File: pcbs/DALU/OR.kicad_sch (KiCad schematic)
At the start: 24 parts

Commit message: Rethinking some design
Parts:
- added U501: 74HCT541, Package_DIP:DIP-20_W7.62mm_Socket, symbol 74xx:74HCT541
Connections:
- net GND: now also U501.10 (GND)
- net OR0: no longer names the net of D501.1 (K), D502.1 (K), R501.1
- net OR0: now also U501.2 (A0)
- net OR1: no longer names the net of D503.1 (K), D504.1 (K), R502.1
- net OR1: now also U501.3 (A1)
- net OR2: no longer names the net of D505.1 (K), D506.1 (K), R503.1
- net OR2: now also U501.4 (A2)
- net OR3: no longer names the net of D507.1 (K), D508.1 (K), R504.1
- net OR3: now also U501.5 (A3)
- net OR4: no longer names the net of D509.1 (K), D510.1 (K), R505.1
- net OR4: now also U501.6 (A4)
- net OR5: no longer names the net of D511.1 (K), D512.1 (K), R506.1
- net OR5: now also U501.7 (A5)
- net OR6: no longer names the net of D513.1 (K), D514.1 (K), R507.1
- net OR6: now also U501.8 (A6)
- net OR7: no longer names the net of D515.1 (K), D516.1 (K), R508.1
- net OR7: now also U501.9 (A7)
- new net +5V: U501.20 (VCC)
- new net ~{ENABLE_{OR}}: U501.1 (G1), U501.19 (G2)

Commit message: Doing some rethinking
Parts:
- removed U501: 74HCT541, Package_DIP:DIP-20_W7.62mm_Socket, symbol 74xx:74HCT541
- added U601: 74HC245, Package_SO:SOIC-20W_7.5x12.8mm_P1.27mm, symbol 74xx:74HC245
- renumbered D501 to D601, D502 to D602, D503 to D603, D504 to D604, D505 to D605, D506 to D606, D507 to D607, D508 to D608, D509 to D609, D510 to D610, D511 to D611, D512 to D612, D513 to D613, D514 to D614, D515 to D615, D516 to D616, R501 to R601, R502 to R602, R503 to R603, R504 to R604, R505 to R605, R506 to R606, R507 to R607, R508 to R608
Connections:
- net +5V: now also U601.20 (VCC)
- net GND: now also U601.10 (GND)
- net at D613.1 (K), D614.1 (K), R607.1: now also U601.8 (A6)
- net at D605.1 (K), D606.1 (K), R603.1: now also U601.4 (A2)
- net at D603.1 (K), D604.1 (K), R602.1: now also U601.3 (A1)
- net at D611.1 (K), D612.1 (K), R606.1: now also U601.7 (A5)
- net at D615.1 (K), D616.1 (K), R608.1: now also U601.9 (A7)
- net at D607.1 (K), D608.1 (K), R604.1: now also U601.5 (A3)
- net at D601.1 (K), D602.1 (K), R601.1: now also U601.2 (A0)
- net at D609.1 (K), D610.1 (K), R605.1: now also U601.6 (A4)

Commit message: Starting to think about decoding etc.
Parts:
- renumbered D601 to D701, D602 to D702, D603 to D703, D604 to D704, D605 to D705, D606 to D706, D607 to D707, D608 to D708, D609 to D709, D610 to D710, D611 to D711, D612 to D712, D613 to D713, D614 to D714, D615 to D715, D616 to D716, R601 to R701, R602 to R702, R603 to R703, R604 to R704, R605 to R705, R606 to R706, R607 to R707, R608 to R708, U601 to U701

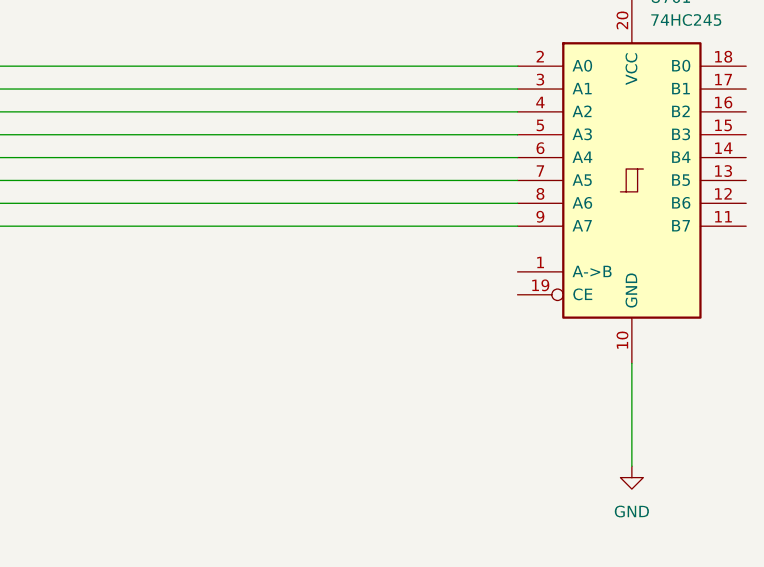
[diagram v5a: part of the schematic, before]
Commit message: Starting to do the routing. Schematic not yet complete, though
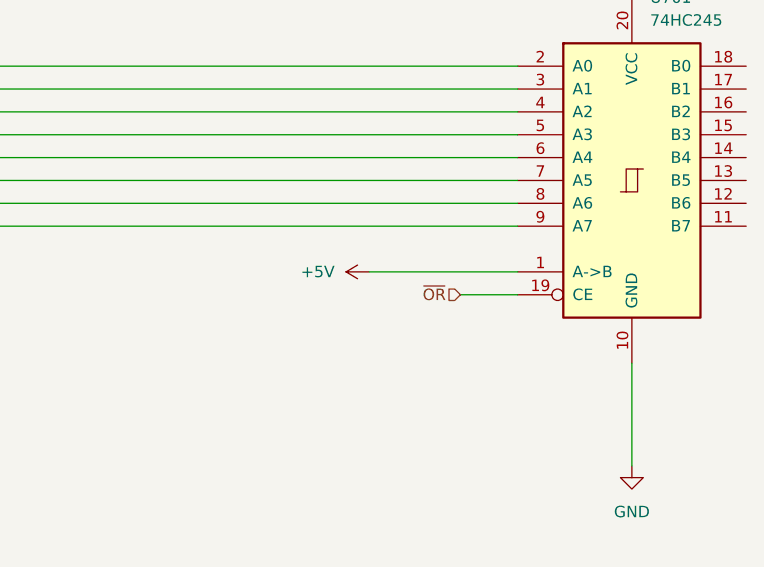
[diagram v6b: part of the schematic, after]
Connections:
- net +5V: now also U701.1 (A->B)
- net ~{OR}: now reaches U701.19 (CE)
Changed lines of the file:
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@@
+    (stroke (width 0) (type default) (color 0 0 0 0))
+  )
+  (wire (pts (xy 214.63 68.58) (xy 220.98 68.58))
     (stroke (width 0) (type default) (color 0 0 0 0))
   )
   (wire (pts (xy 83.82 52.07) (xy 91.44 52.07))
+    (stroke (width 0) (type default) (color 0 0 0 0))
+  )
+  (wire (pts (xy 204.47 66.04) (xy 220.98 66.04))
     (stroke (width 0) (type default) (color 0 0 0 0))
   )
@@
   )
   (hierarchical_label "B[0..7]" (shape input) (at 38.1 30.48 180)
+    (effects (font (size 1.27 1.27)) (justify right))
+  )
+  (hierarchical_label "~{OR}" (shape input) (at 214.63 68.58 180)
     (effects (font (size 1.27 1.27)) (justify right))
   )
@@
     (pin "2")
   )
+  (symbol (lib_id "power:+5V") (at 204.47 66.04 90) (unit 1)
+    (in_bom yes) (on_board yes) (fields_autoplaced)
+    (property "Reference" "#PWR0103" (id 0) (at 208.28 66.04 0)
+      (effects (font (size 1.27 1.27)) hide)
+    )
+    (property "Value" "+5V" (id 1) (at 200.66 66.0399 90)
+      (effects (font (size 1.27 1.27)) (justify left))
+    )
+    (property "Footprint" "" (id 2) (at 204.47 66.04 0)
+      (effects (font (size 1.27 1.27)) hide)
+    )
+    (property "Datasheet" "" (id 3) (at 204.47 66.04 0)
+      (effects (font (size 1.27 1.27)) hide)
+    )
+    (pin "1")
+  )
   (symbol (lib_id "Diode:1N4148") (at 80.01 128.27 180) (unit 1)

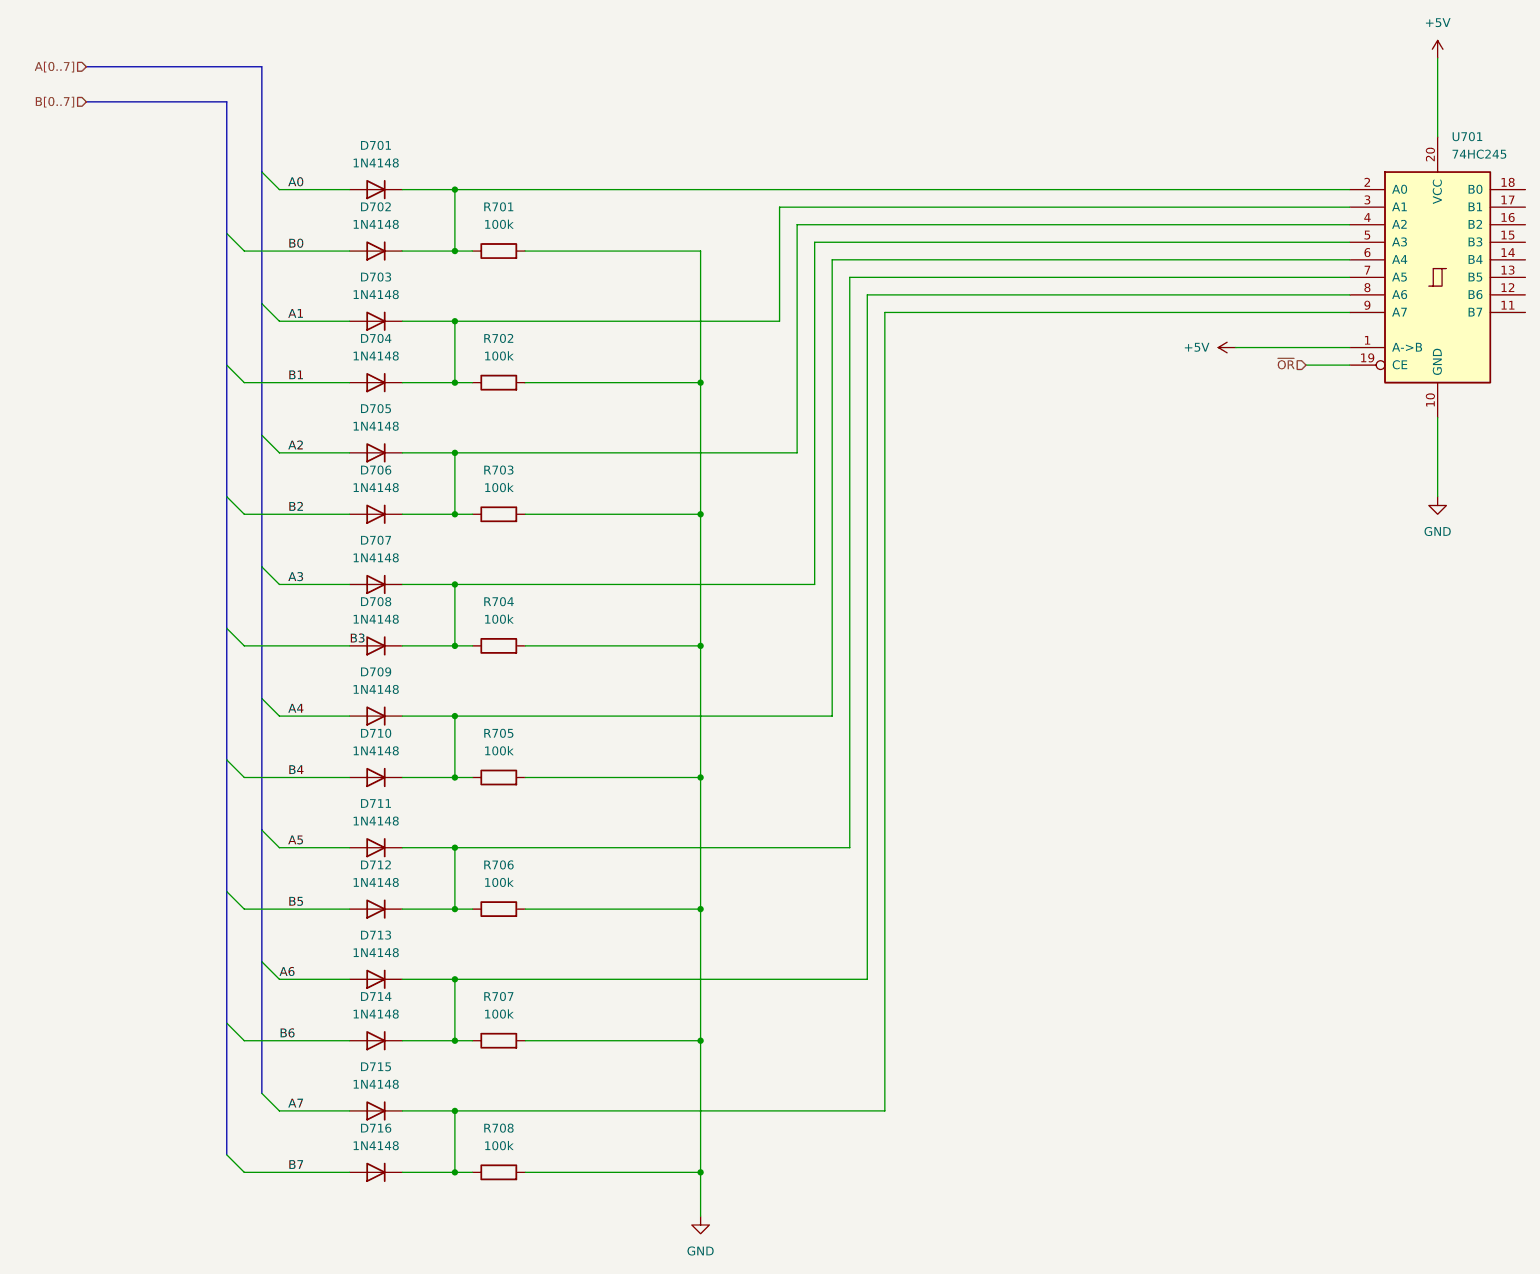
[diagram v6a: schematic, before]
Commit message: Removing diode ORs (mainly). Preparing for a small rethink
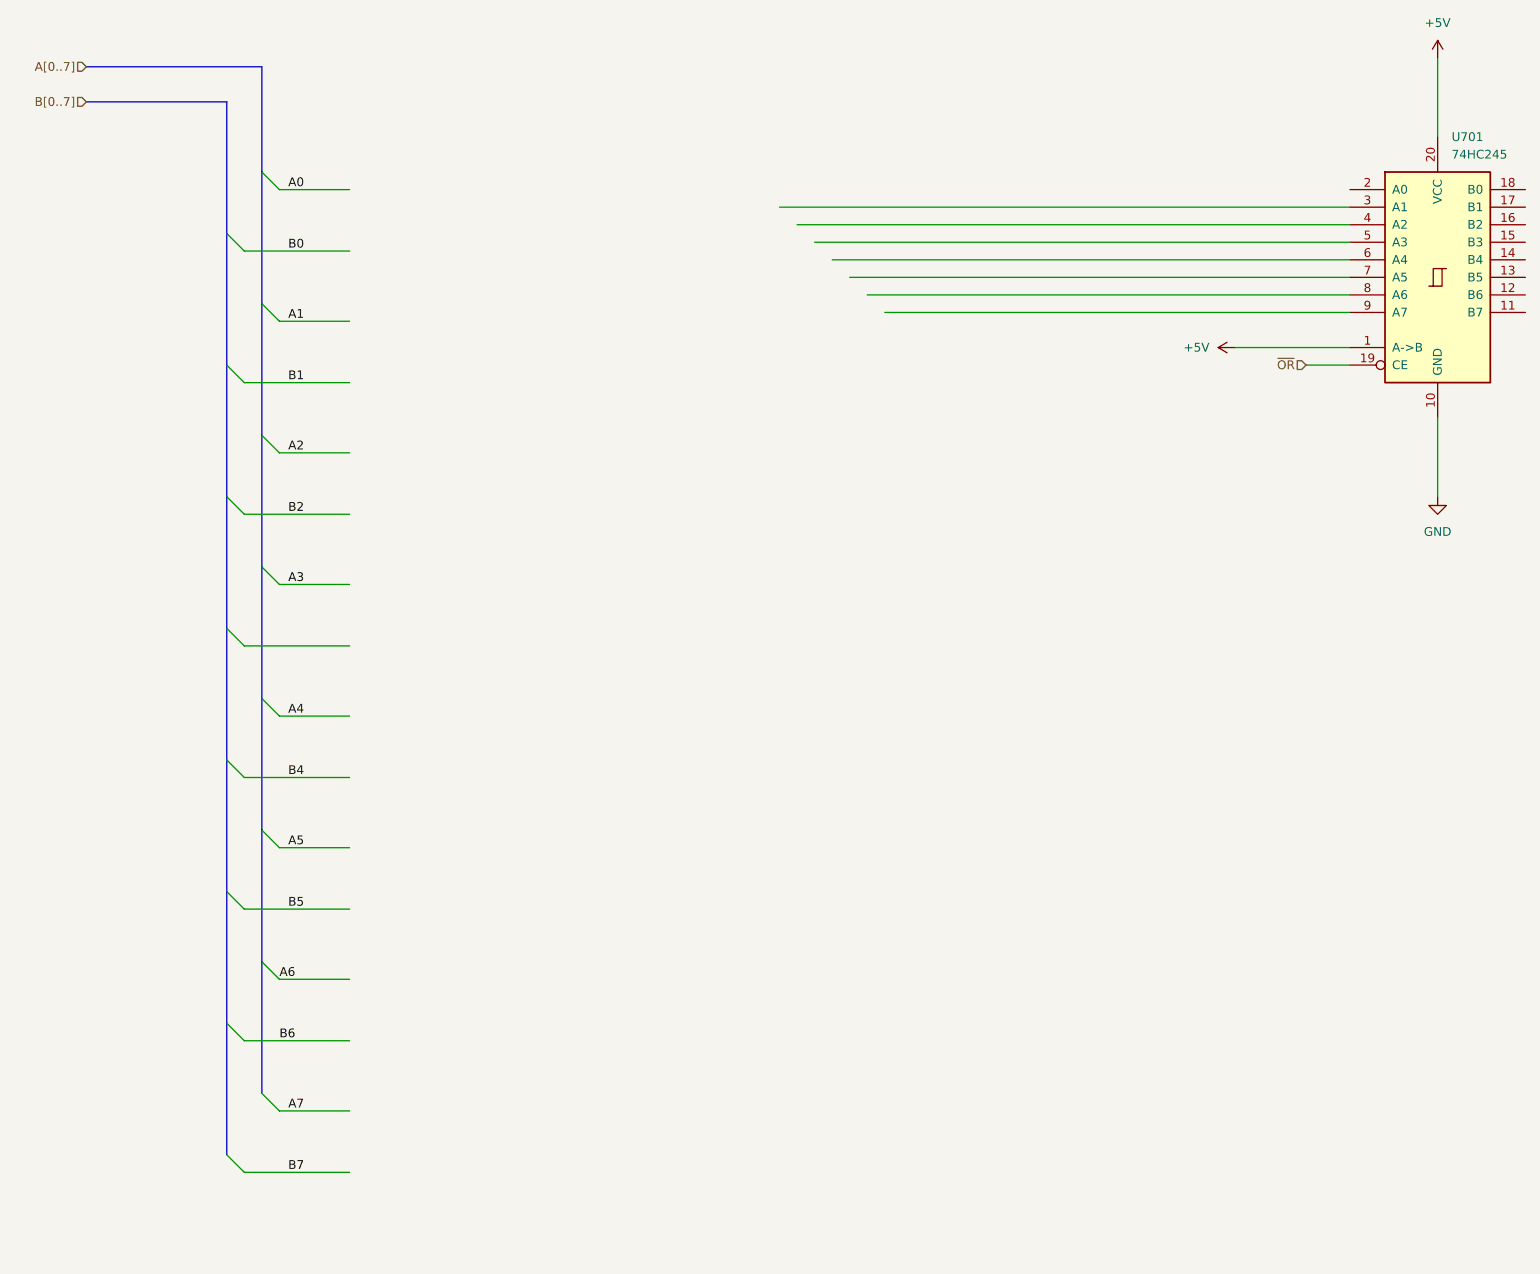
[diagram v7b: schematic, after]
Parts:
- removed D701, D702, D703, D704, D705, D706, D707, D708, D709, D710, D711, D712, D713, D714, D715, D716: 1N4148, Diode_THT:D_DO-35_SOD27_P7.62mm_Horizontal, symbol Diode:1N4148
- removed R701, R702, R703, R704, R705, R706, R707, R708: 100k, Resistor_THT:R_Axial_DIN0207_L6.3mm_D2.5mm_P7.62mm_Horizontal, symbol Device:R

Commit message: Separate out AND stage
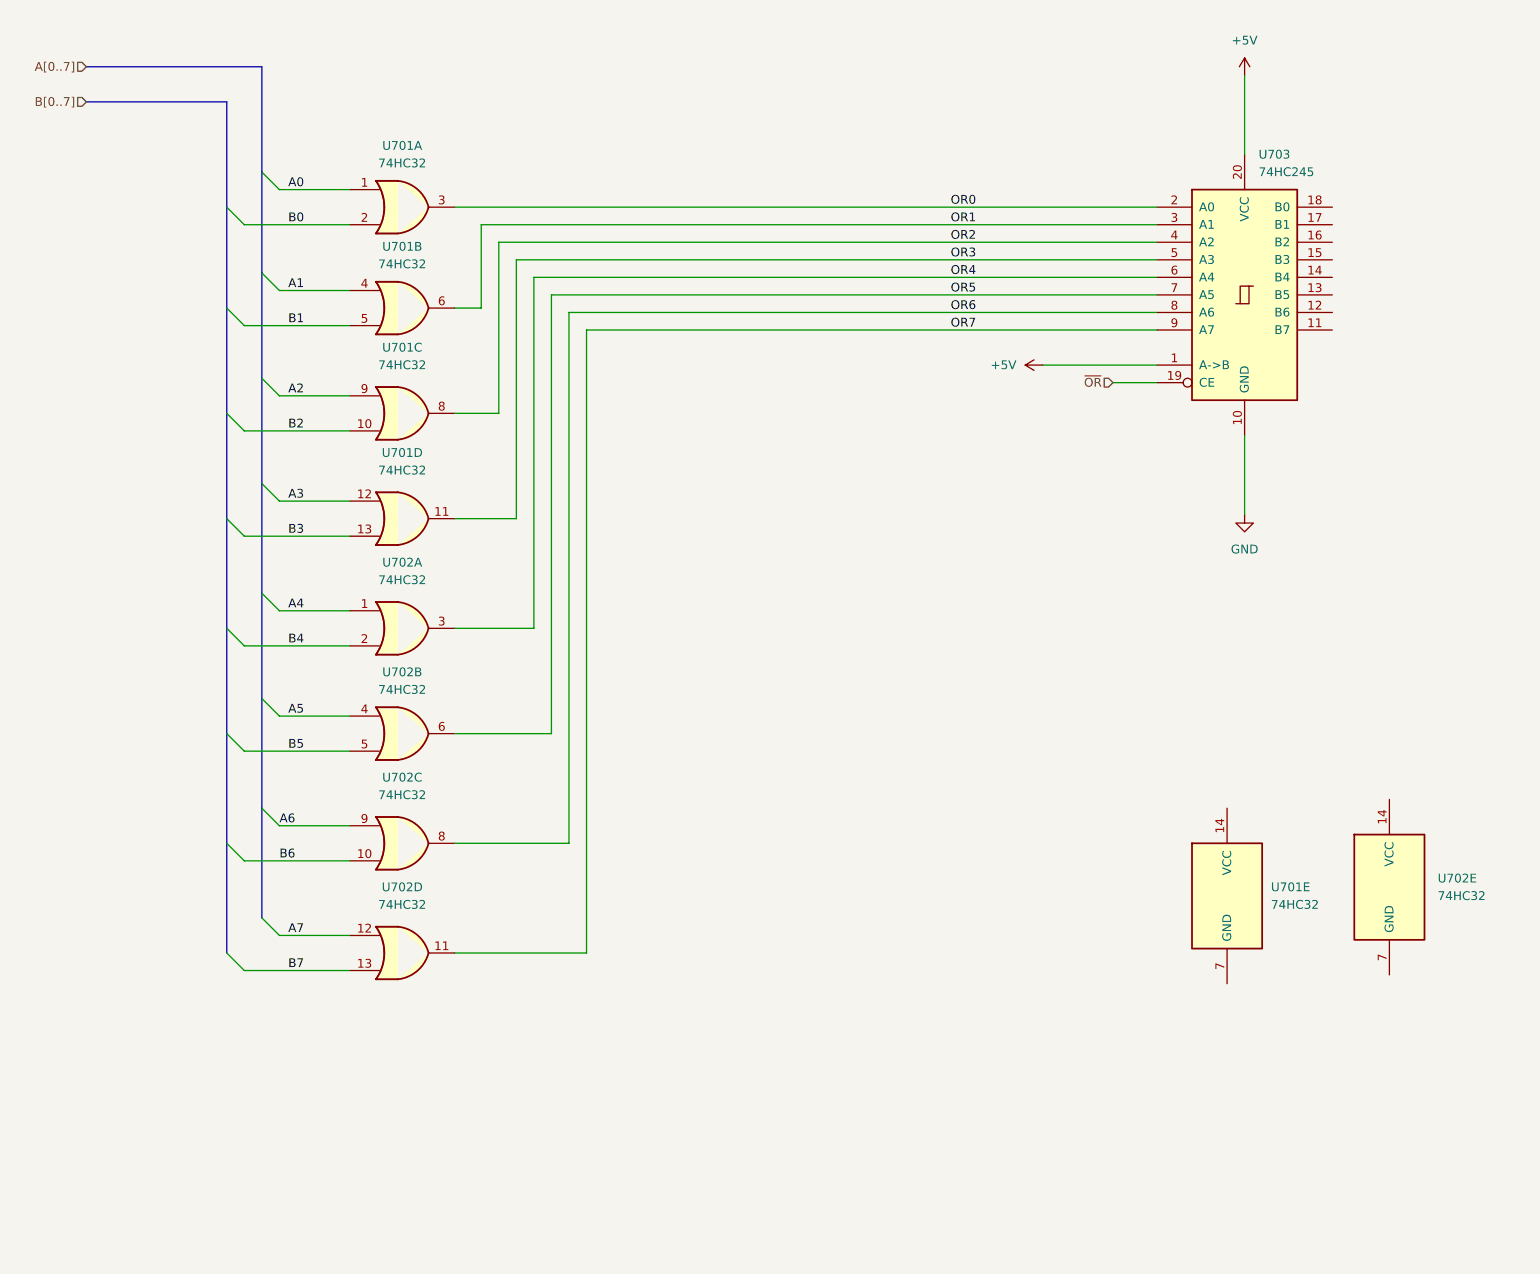
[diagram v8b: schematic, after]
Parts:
- added U701, U702: 74HC32, Package_DIP:DIP-14_W7.62mm_Socket, symbol 74xx:74LS32
- renumbered U701 to U703
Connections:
- net A0: now also U701.1
- net A1: now also U701.4
- net A2: now also U701.9
- net A3: now also U701.12
- net A4: now also U702.1
- net A5: now also U702.4
- net A6: now also U702.9
- net A7: now also U702.12
- net B0: now also U701.2
- net B1: now also U701.5
- net B2: now also U701.10
- net B4: now also U702.2
- net B5: now also U702.5
- net B6: now also U702.10
- net B7: now also U702.13
- net OR0: now reaches U703.2 (A0)
- net OR0: now also U701.3
- net OR1: now reaches U703.3 (A1)
- net OR1: now also U701.6
- net OR2: now reaches U703.4 (A2)
- net OR2: now also U701.8
- net OR3: now reaches U703.5 (A3)
- net OR3: now also U701.11
- net OR4: now reaches U703.6 (A4)
- net OR4: now also U702.3
- net OR5: now reaches U703.7 (A5)
- net OR5: now also U702.6
- net OR6: now reaches U703.8 (A6)
- net OR6: now also U702.8
- net OR7: now reaches U703.9 (A7)
- net OR7: now also U702.11
- new net B3: U701.13
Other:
- moved on the sheet: U703
